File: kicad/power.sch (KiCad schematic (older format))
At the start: 6 parts, among them T1 TLV61225DCKR

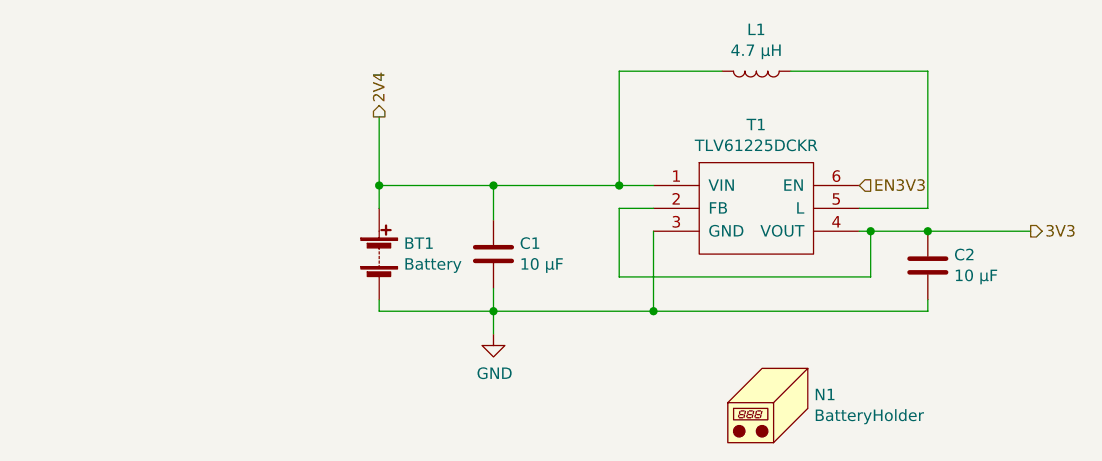
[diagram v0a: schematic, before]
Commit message: added reverse polarization protection
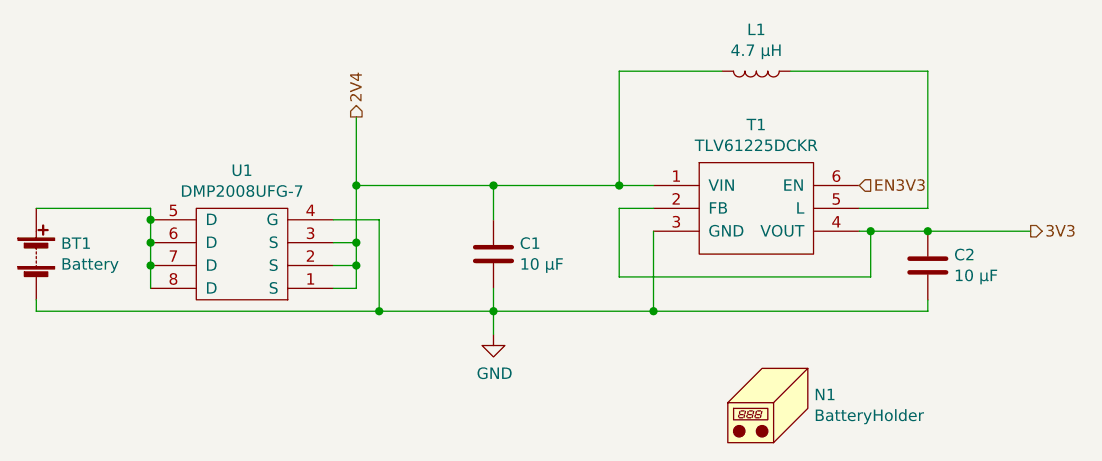
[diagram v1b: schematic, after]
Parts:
- added U1: DMP2008UFG-7, data-logger:DMP2008UFG-7, symbol data-logger:DMP2008UFG-7
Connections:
- net 2V4: now also U1.1 (S), U1.2 (S), U1.3 (S); no longer BT1.1 (+)
- net GND: now also U1.4 (G)
- new net: BT1.1 (+), U1.5 (D), U1.6 (D), U1.7 (D), U1.8 (D)
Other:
- moved on the sheet: BT1
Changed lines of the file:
@@
 	6100 2950 5650 2950
 Connection ~ 5650 2950
-Text HLabel 3250 2450 1    50   Output ~ 0
+Text HLabel 3150 2450 1    50   Output ~ 0
 2V4
 Connection ~ 3750 2750
@@
 L Device:Battery BT1
 U 1 1 5EC99AE6
-P 3250 3050
-F 0 "BT1" H 3358 3096 50  0000 L CNN
-F 1 "Battery" H 3358 3005 50  0000 L CNN
-F 2 "Connector_PinSocket_2.54mm:PinSocket_1x02_P2.54mm_Horizontal" V 3250 3110 50  0001 C CNN
-F 3 "http://www.memoryprotectiondevices.com/datasheets/BC2AAAL-datasheet.pdf" V 3250 3110 50  0001 C CNN
-F 4 "BC2AAAL-ND" H 3250 3050 50  0001 C CNN "DigiKey_PartNumber"
-	1    3250 3050
+P 1750 3050
+F 0 "BT1" H 1858 3096 50  0000 L CNN
+F 1 "Battery" H 1858 3005 50  0000 L CNN
+F 2 "Connector_PinSocket_2.54mm:PinSocket_1x02_P2.54mm_Horizontal" V 1750 3110 50  0001 C CNN
+F 3 "http://www.memoryprotectiondevices.com/datasheets/BC2AAAL-datasheet.pdf" V 1750 3110 50  0001 C CNN
+F 4 "BC2AAAL-ND" H 1750 3050 50  0001 C CNN "DigiKey_PartNumber"
+	1    1750 3050
 	1    0    0    -1
 $EndComp
-Wire Wire Line
-	3250 2450 3250 2750
-Wire Wire Line
-	3250 2750 3750 2750
-Connection ~ 3250 2750
-Wire Wire Line
-	3250 2750 3250 2850
-Wire Wire Line
-	3250 3250 3250 3300
 Wire Wire Line
 	3250 3300 3750 3300
@@
 	1    0    0    -1
 $EndComp
+$Comp
+L data-logger:DMP2008UFG-7 U1
+U 1 1 5ECAF515
+P 2650 3050
+F 0 "U1" H 2650 2685 50  0000 C CNN
+F 1 "DMP2008UFG-7" H 2650 2776 50  0000 C CNN
+F 2 "data-logger:DMP2008UFG-7" H 2650 2500 50  0001 C CNN
+F 3 "https://www.diodes.com/assets/Datasheets/DMP2008UFG.pdf" H 2650 3050 50  0001 C CNN
+F 4 "DMP2008UFG-7DICT-ND" H 2650 2600 50  0001 C CNN "DigiKey_PartNumber"
+	1    2650 3050
+	-1   0    0    1
+$EndComp
+Wire Wire Line
+	1750 2850 2250 2850
+Wire Wire Line
+	2250 2850 2250 2900
+Wire Wire Line
+	2250 2900 2250 3000
+Connection ~ 2250 2900
+Wire Wire Line
+	2250 3000 2250 3100
+Connection ~ 2250 3000
+Wire Wire Line
+	2250 3100 2250 3200
+Connection ~ 2250 3100
+Wire Wire Line
+	3250 3300 3250 2900
+Wire Wire Line
+	3250 2900 3050 2900
+Wire Wire Line
+	3250 3300 1750 3300
+Wire Wire Line
+	1750 3300 1750 3250
+Connection ~ 3250 3300
+Wire Wire Line
+	3150 2750 3150 2450
+Wire Wire Line
+	3150 2750 3750 2750
+Wire Wire Line
+	3150 2750 3150 3000
+Wire Wire Line
+	3150 3200 3050 3200
+Connection ~ 3150 2750
+Wire Wire Line
+	3050 3100 3150 3100
+Connection ~ 3150 3100
+Wire Wire Line
+	3150 3100 3150 3200
+Wire Wire Line
+	3050 3000 3150 3000
+Connection ~ 3150 3000
+Wire Wire Line
+	3150 3000 3150 3100
 $EndSCHEMATC

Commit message: tweaks after drc
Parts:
- BT1: footprint Connector_PinSocket_2.54mm:PinSocket_1x02_P2.54mm_Horizontal -> data-logger:PinSocket_1x02_P2.54mm_Horizontal; DigiKey_PartNumber BC2AAAL-ND -> SAM1225-02-ND
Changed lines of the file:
@@
 F 0 "BT1" H 1858 3096 50  0000 L CNN
 F 1 "Battery" H 1858 3005 50  0000 L CNN
-F 2 "Connector_PinSocket_2.54mm:PinSocket_1x02_P2.54mm_Horizontal" V 1750 3110 50  0001 C CNN
-F 3 "http://www.memoryprotectiondevices.com/datasheets/BC2AAAL-datasheet.pdf" V 1750 3110 50  0001 C CNN
-F 4 "BC2AAAL-ND" H 1750 3050 50  0001 C CNN "DigiKey_PartNumber"
+F 2 "data-logger:PinSocket_1x02_P2.54mm_Horizontal" V 1750 3110 50  0001 C CNN
+F 3 "http://suddendocs.samtec.com/catalog_english/ssw_th.pdf" V 1750 3110 50  0001 C CNN
+F 4 "SAM1225-02-ND" H 1750 3050 50  0001 C CNN "DigiKey_PartNumber"
 	1    1750 3050
 	1    0    0    -1
